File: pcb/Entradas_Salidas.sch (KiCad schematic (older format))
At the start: 15 parts, among them U10 VOM617A, U11 VOM617A, U12 ASSR-1218, U13 ASSR-1218, U9 VOM617A

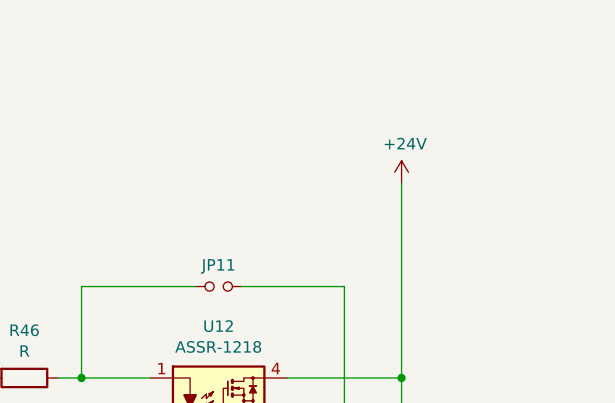
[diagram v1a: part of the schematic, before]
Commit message: añadidos led para estado y alimentacion externa para salidas digitales
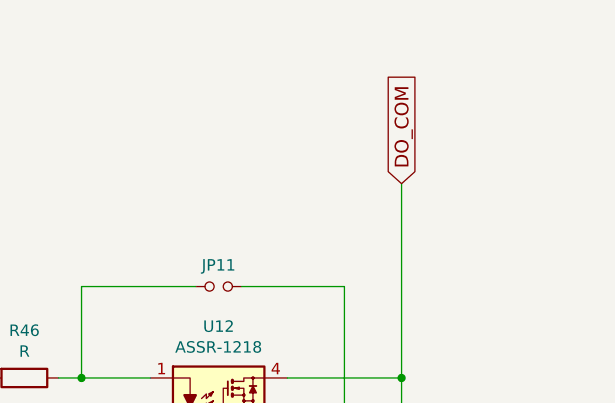
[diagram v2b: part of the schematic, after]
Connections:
- net +24V renamed DO_COM
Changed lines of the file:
@@
 Connection ~ 8450 4600
 $Comp
-L GND #PWR0104
+L GND #PWR0107
 U 1 1 57843D7F
 P 8450 5000
-F 0 "#PWR0104" H 8450 4750 50  0001 C CNN
+F 0 "#PWR0107" H 8450 4750 50  0001 C CNN
 F 1 "GND" H 8455 4827 50  0000 C CNN
 F 2 "" H 8450 5000 50  0000 C CNN
@@
 	2700 2750 2700 5400
 $Comp
-L GND #PWR0105
+L GND #PWR0108
 U 1 1 5784404E
 P 2700 5400
-F 0 "#PWR0105" H 2700 5150 50  0001 C CNN
+F 0 "#PWR0108" H 2700 5150 50  0001 C CNN
 F 1 "GND" H 2705 5227 50  0000 C CNN
 F 2 "" H 2700 5400 50  0000 C CNN
@@
 	3950 4900 3950 1800
 $Comp
-L +5V #PWR0106
+L +5V #PWR0109
 U 1 1 57844144
 P 3950 1800
-F 0 "#PWR0106" H 3950 1650 50  0001 C CNN
+F 0 "#PWR0109" H 3950 1650 50  0001 C CNN
 F 1 "+5V" H 3965 1973 50  0000 C CNN
 F 2 "" H 3950 1800 50  0000 C CNN
@@
 	8250 2750 8250 3150
 Connection ~ 8250 3150
-$Comp
-L +24V #PWR0107
-U 1 1 57845312
-P 9650 2300
-F 0 "#PWR0107" H 9650 2150 50  0001 C CNN
-F 1 "+24V" H 9665 2473 50  0000 C CNN
-F 2 "" H 9650 2300 50  0000 C CNN
-F 3 "" H 9650 2300 50  0000 C CNN
-	1    9650 2300
-	1    0    0    -1
-$EndComp
 Wire Wire Line
 	8950 2750 9400 2750
@@
 Text GLabel 10150 4600 2    60   Output ~ 0
 DO2
+Text GLabel 9650 2300 1    60   Input ~ 0
+DO_COM
 $EndSCHEMATC
